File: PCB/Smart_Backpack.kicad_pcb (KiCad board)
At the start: 2 copper layers, 2 parts, among them J1 Power USB C Receptacle, U2 ICM-20602

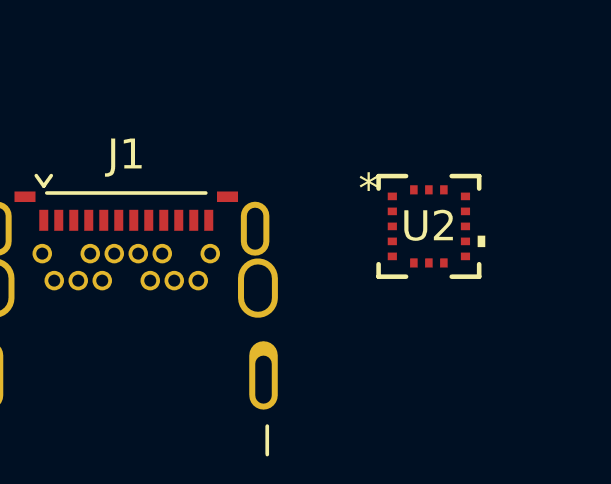
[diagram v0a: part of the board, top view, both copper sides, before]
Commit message: New IMU symbol/footprint
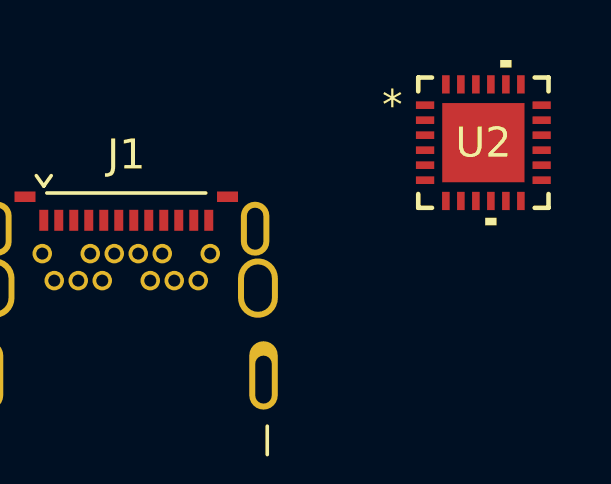
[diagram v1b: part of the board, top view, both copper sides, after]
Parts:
- U2: value ICM-20602 -> MPU-6050; footprint IMU:LGA16_I62_IVS-L -> IMU:QFN24_4X4X0P9-0P5_TDK-L
- moved U2 3.33 mm to (94.6, 74.9)

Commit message: Added micro footprint
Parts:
- added U3: ESP32-PICO-MINI-02-N8R2, STM32:ESP32-PICO-MINI-02_EXP, F.Cu at (57.6, 53.3)

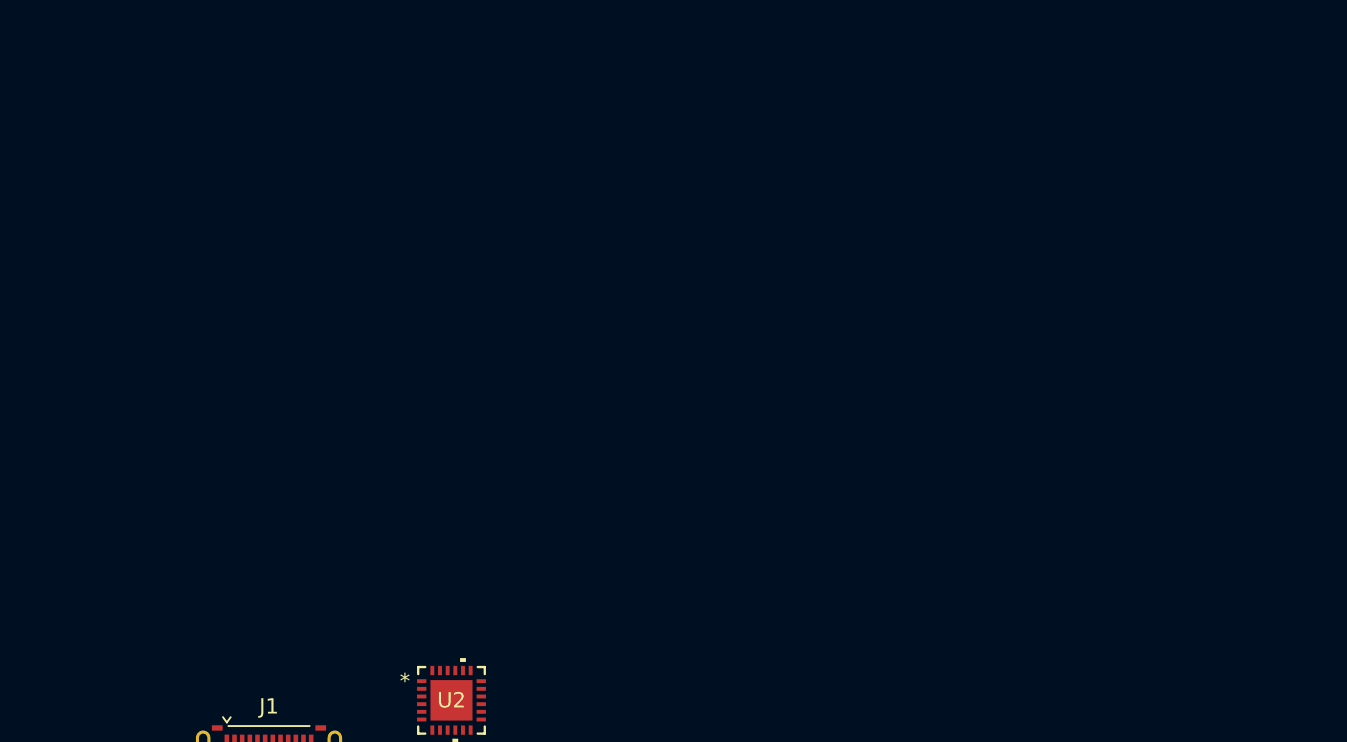
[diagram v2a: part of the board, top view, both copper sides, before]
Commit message: add pressure button and R, C, and L footprints
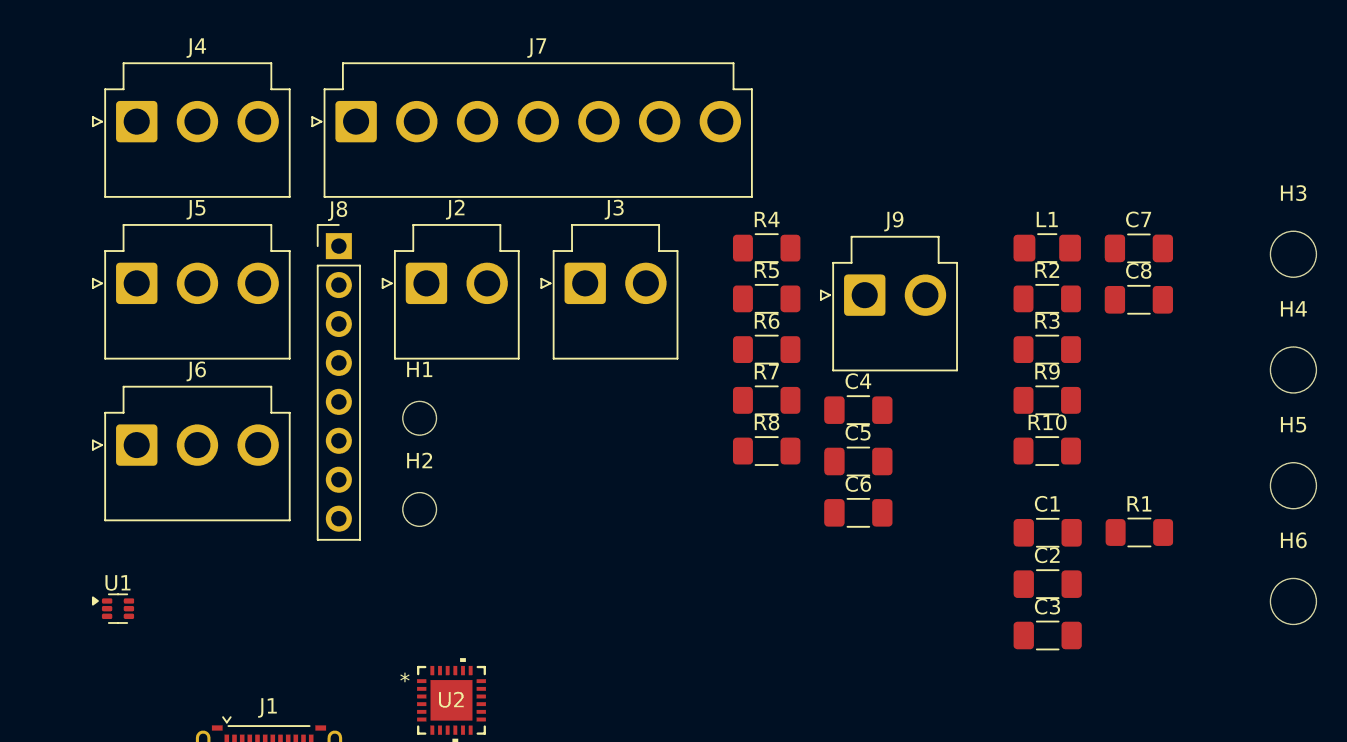
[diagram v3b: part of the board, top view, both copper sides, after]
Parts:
- added C1: 22uF, Capacitor_SMD:C_1206_3216Metric_Pad1.33x1.80mm_HandSolder, F.Cu at (133.5, 64.0)
- added C2: 0.1uF, Capacitor_SMD:C_1206_3216Metric_Pad1.33x1.80mm_HandSolder, F.Cu at (133.5, 67.4)
- added C3: 1uF, Capacitor_SMD:C_1206_3216Metric_Pad1.33x1.80mm_HandSolder, F.Cu at (133.5, 70.7)
- added C4: 2.2nF, Capacitor_SMD:C_1206_3216Metric_Pad1.33x1.80mm_HandSolder, F.Cu at (121.1, 56.0)
- added C5: 0.1uF, Capacitor_SMD:C_1206_3216Metric_Pad1.33x1.80mm_HandSolder, F.Cu at (121.1, 59.4)
- added C6: 10uF, Capacitor_SMD:C_1206_3216Metric_Pad1.33x1.80mm_HandSolder, F.Cu at (121.1, 62.7)
- added C7: 4.7uF, Capacitor_SMD:C_1206_3216Metric_Pad1.33x1.80mm_HandSolder, F.Cu at (139.4, 45.5)
- added C8: 22uF, Capacitor_SMD:C_1206_3216Metric_Pad1.33x1.80mm_HandSolder, F.Cu at (139.4, 48.8)
- added H1: MountingHole, MountingHole:MountingHole_2.2mm_M2, F.Cu at (92.5, 56.5)
- added H2: MountingHole, MountingHole:MountingHole_2.2mm_M2, F.Cu at (92.5, 62.5)
- added H3: MountingHole, MountingHole:MountingHole_3mm, F.Cu at (149.5, 45.9)
- added H4: MountingHole, MountingHole:MountingHole_3mm, F.Cu at (149.5, 53.4)
- added H5: MountingHole, MountingHole:MountingHole_3mm, F.Cu at (149.5, 61.0)
- added H6: MountingHole, MountingHole:MountingHole_3mm, F.Cu at (149.5, 68.5)
- added J2: Conn_01x02_Pin, Connector_JST:JST_VH_B2P-VH_1x02_P3.96mm_Vertical, F.Cu at (92.9, 47.8)
- added J3: Conn_01x02_Pin, Connector_JST:JST_VH_B2P-VH_1x02_P3.96mm_Vertical, F.Cu at (103.3, 47.8)
- added J4: Conn_01x03_Pin, Connector_JST:JST_VH_B3P-VH_1x03_P3.96mm_Vertical, F.Cu at (74.0, 37.2)
- added J5: Conn_01x03_Pin, Connector_JST:JST_VH_B3P-VH_1x03_P3.96mm_Vertical, F.Cu at (74.0, 47.8)
- added J6: Conn_01x03_Pin, Connector_JST:JST_VH_B3P-VH_1x03_P3.96mm_Vertical, F.Cu at (74.0, 58.3)
- added J7: Conn_01x07_Pin, Connector_JST:JST_VH_B7P-VH_1x07_P3.96mm_Vertical, F.Cu at (88.4, 37.2)
- added J8: Conn_01x08_Socket, Connector_PinHeader_2.54mm:PinHeader_1x08_P2.54mm_Vertical, F.Cu at (87.2, 45.3)
- added J9: Conn_01x02_Pin, Connector_JST:JST_VH_B2P-VH_1x02_P3.96mm_Vertical, F.Cu at (121.5, 48.5)
- added L1: 1uH, Inductor_SMD:L_1206_3216Metric_Pad1.42x1.75mm_HandSolder, F.Cu at (133.4, 45.5)
- added R1: 10 kΩ, Resistor_SMD:R_1206_3216Metric_Pad1.30x1.75mm_HandSolder, F.Cu at (139.4, 64.0)
- added R10: 5.1kΩ, Resistor_SMD:R_1206_3216Metric_Pad1.30x1.75mm_HandSolder, F.Cu at (133.4, 58.7)
- added R2: 5.1kΩ, Resistor_SMD:R_1206_3216Metric_Pad1.30x1.75mm_HandSolder, F.Cu at (133.4, 48.8)
- added R3: 5.1kΩ, Resistor_SMD:R_1206_3216Metric_Pad1.30x1.75mm_HandSolder, F.Cu at (133.4, 52.1)
- added R4: 10kΩ, Resistor_SMD:R_1206_3216Metric_Pad1.30x1.75mm_HandSolder, F.Cu at (115.1, 45.5)
- added R5: 10kΩ, Resistor_SMD:R_1206_3216Metric_Pad1.30x1.75mm_HandSolder, F.Cu at (115.1, 48.8)
- added R6: 10K, Resistor_SMD:R_1206_3216Metric_Pad1.30x1.75mm_HandSolder, F.Cu at (115.1, 52.1)
- added R7: 10K, Resistor_SMD:R_1206_3216Metric_Pad1.30x1.75mm_HandSolder, F.Cu at (115.1, 55.4)
- added R8: 10K, Resistor_SMD:R_1206_3216Metric_Pad1.30x1.75mm_HandSolder, F.Cu at (115.1, 58.7)
- added R9: 5.1kΩ, Resistor_SMD:R_1206_3216Metric_Pad1.30x1.75mm_HandSolder, F.Cu at (133.4, 55.4)
- added U1: TLV62569ADRL, Package_TO_SOT_SMD:SOT-563, F.Cu at (72.8, 69.0)
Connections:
- U2 pad 10: unconnected-(U2-REGOUT-Pad10) -> Net-(U2-REGOUT)
- U2 pad 12: unconnected-(U2-INT-Pad12) -> IMU_INT
- U2 pad 13: unconnected-(U2-VDD-Pad13) -> Buck_3v3
- U2 pad 18: unconnected-(U2-GND-Pad18) -> GND
- U2 pad 20: unconnected-(U2-CPOUT-Pad20) -> Net-(U2-CPOUT)
- U2 pad 23: unconnected-(U2-SCL-Pad23) -> ESP_SCL
- U2 pad 24: unconnected-(U2-SDA-Pad24) -> ESP_SDA
- U2 pad 25: unconnected-(U2-EPAD-Pad25) -> GND
- U2 pad 8: unconnected-(U2-VLOGIC-Pad8) -> Buck_3v3

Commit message: lots of 'final' schematic updates. ERC is essentially clean, PCB design can begin
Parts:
- added C10: 0.1uF, Capacitor_SMD:C_1206_3216Metric_Pad1.33x1.80mm_HandSolder, F.Cu at (182.2, 50.2)
- added C11: 0.1uF, Capacitor_SMD:C_1206_3216Metric_Pad1.33x1.80mm_HandSolder, F.Cu at (182.2, 53.6)
- added C12: 15pF, Capacitor_SMD:C_1206_3216Metric_Pad1.33x1.80mm_HandSolder, F.Cu at (156.0, 26.5)
- added C13: 15pF, Capacitor_SMD:C_1206_3216Metric_Pad1.33x1.80mm_HandSolder, F.Cu at (156.0, 29.9)
- added C9: 0.1uF, Capacitor_SMD:C_1206_3216Metric_Pad1.33x1.80mm_HandSolder, F.Cu at (193.5, 55.5)
- added D1: 3v3 Indicator, LED_SMD:LED_0603_1608Metric_Pad1.05x0.95mm_HandSolder, F.Cu at (181.4, 56.5)
- added D2: 5V Indicator, LED_SMD:LED_0603_1608Metric_Pad1.05x0.95mm_HandSolder, F.Cu at (181.4, 59.1)
- added J1: Conn_01x03_Pin, Connector_JST:JST_VH_B3P-VH_1x03_P3.96mm_Vertical, F.Cu at (193.9, 40.3)
- added R11: Minimum Resistance, Resistor_SMD:R_1206_3216Metric_Pad1.30x1.75mm_HandSolder, F.Cu at (192.9, 79.5)
- added R12: 5.1kΩ, Resistor_SMD:R_1206_3216Metric_Pad1.30x1.75mm_HandSolder, F.Cu at (207.6, 69.1)
- added R13: 5.1kΩ, Resistor_SMD:R_1206_3216Metric_Pad1.30x1.75mm_HandSolder, F.Cu at (207.6, 72.4)
- added R14: 47.5kΩ, Resistor_SMD:R_1206_3216Metric_Pad1.30x1.75mm_HandSolder, F.Cu at (207.6, 75.7)
- added R15: 1MΩ, Resistor_SMD:R_1206_3216Metric_Pad1.30x1.75mm_HandSolder, F.Cu at (207.6, 79.0)
- added R16: 10kΩ, Resistor_SMD:R_1206_3216Metric_Pad1.30x1.75mm_HandSolder, F.Cu at (207.6, 82.3)
- added R17: Minimum Resistance, Resistor_SMD:R_1206_3216Metric_Pad1.30x1.75mm_HandSolder, F.Cu at (207.6, 85.6)
- added R18: 10MΩ, Resistor_SMD:R_1206_3216Metric_Pad1.30x1.75mm_HandSolder, F.Cu at (201.4, 87.0)
- added R19: 150Ω, Resistor_SMD:R_1206_3216Metric_Pad1.30x1.75mm_HandSolder, F.Cu at (207.6, 88.9)
- added R20: 330Ω, Resistor_SMD:R_1206_3216Metric_Pad1.30x1.75mm_HandSolder, F.Cu at (207.6, 92.2)
- added RTC1: 32.768kHz, RTC:XTAL_AB38T-32.768KHZ-B7, F.Cu at (163.5, 22.5)
- added SW1: SW_Push, SMD_Button:Shop_SMD_Button, F.Cu at (195.1, 51.0)
- added SW2: SW_Push, SMD_Button:Shop_SMD_Button, F.Cu at (183.8, 38.5)
- added U4: CP2102N-Axx-xQFN28, Package_DFN_QFN:QFN-28-1EP_5x5mm_P0.5mm_EP3.35x3.35mm, F.Cu at (182.8, 44.9)
- R2: value 5.1kΩ -> 2kΩ
- R3: value 5.1kΩ -> 22.1kΩ
- moved R8 64.7 mm to (176.4, 79.5)
- moved R7 60.8 mm to (170.9, 79.5)
- moved R10 58.0 mm to (187.6, 79.5)
- moved R6 57.3 mm to (165.4, 79.5)
- moved R5 54.3 mm to (159.9, 79.5)
- moved R9 54.2 mm to (182.0, 79.5)
- moved R4 52.0 mm to (154.4, 79.5)
- moved R2 32.2 mm to (142.9, 79.5)
- moved R3 31.5 mm to (148.9, 79.5)
- moved R1 15.6 mm to (137.4, 79.5)
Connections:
- C1 pad 1: Buck_3v3 -> +3V3
- C2 pad 1: Buck_3v3 -> +3V3
- C6 pad 1: Buck_3v3 -> +3V3
- C7 pad 1: USB_5V -> +5V
- C8 pad 1: Buck_3v3 -> +3V3
- J2 pad 1: /Peripherals/FLEX_1 -> FLEX_1
- J3 pad 1: /Peripherals/FLEX_2 -> FLEX_2
- J4 pad 2: /Peripherals/MOIST_SIG -> MOIST_SIG
- J5 pad 2: /Peripherals/HALL_1 -> HALL_1
- J6 pad 2: /Peripherals/HALL_2 -> HALL_2
- J7 pad 2: /Peripherals/SS -> RFID_CS
- J7 pad 3: /Peripherals/SCK -> RFID_SCLK
- J7 pad 4: /Peripherals/MOSI -> RFID_MOSI
- J7 pad 5: /Peripherals/MISO -> RFID_MISO
- J7 pad 6: /Peripherals/SPI_RST -> RFID_RST
- J8 pad 5: unconnected-(J8-Pin_5-Pad5) -> GPS_TX
- J8 pad 6: unconnected-(J8-Pin_6-Pad6) -> GPS_RX
- J8 pad 7: unconnected-(J8-Pin_7-Pad7) -> GND
- J8 pad 8: unconnected-(J8-Pin_8-Pad8) -> +3V3
- L1 pad 2: Buck_3v3 -> +3V3
- R1 pad 1: Buck_3v3 -> +3V3
- R2 pad 1: Net-(J1-CC1) -> +3V3
- R2 pad 2: GND -> Net-(U4-~{RST})
- R3 pad 1: Net-(J1-CC2) -> Net-(U4-VBUS)
- R3 pad 2: GND -> +5V
- R4 pad 1: Buck_3v3 -> +3V3
- R4 pad 2: ESP_SDA -> IMU_SDA
- R5 pad 1: Buck_3v3 -> +3V3
- R5 pad 2: ESP_SCL -> IMU_SCL
- R6 pad 1: /Peripherals/FLEX_1 -> FLEX_1
- R7 pad 1: /Peripherals/FLEX_2 -> FLEX_2
- R8 pad 1: /Peripherals/MOIST_SIG -> MOIST_SIG
- R9 pad 1: Buck_3v3 -> +3V3
- U1 pad 3: USB_5V -> +5V
- U1 pad 5: USB_5V -> +5V
- U2 pad 13: Buck_3v3 -> +3V3
- U2 pad 23: ESP_SCL -> IMU_SCL
- U2 pad 24: ESP_SDA -> IMU_SDA
- U2 pad 8: Buck_3v3 -> +3V3
- U3 pad 10: unconnected-(U3-I35-Pad10) -> MOIST_SIG
- U3 pad 12: unconnected-(U3-IO32-Pad12) -> RTC_XP
- U3 pad 13: unconnected-(U3-IO33-Pad13) -> RTC_XN
- U3 pad 15: unconnected-(U3-IO25-Pad15) -> LAPTOP
- U3 pad 17: unconnected-(U3-IO27-Pad17) -> RFID_RST
- U3 pad 18: unconnected-(U3-IO14-Pad18) -> RFID_SCLK
- U3 pad 19: unconnected-(U3-IO12-Pad19) -> RFID_MISO
- U3 pad 20: unconnected-(U3-IO13-Pad20) -> RFID_MOSI
- U3 pad 21: unconnected-(U3-IO15-Pad21) -> RFID_CS
- U3 pad 23: unconnected-(U3-IO0-Pad23) -> IO0
- U3 pad 26: unconnected-(U3-IO20-Pad26) -> IMU_SCL
- U3 pad 27: unconnected-(U3-IO7-Pad27) -> GPS_TX
- U3 pad 28: unconnected-(U3-IO8-Pad28) -> GPS_RX
- U3 pad 3: Buck_3v3 -> +3V3
- U3 pad 30: unconnected-(U3-RXD0-Pad30) -> Flash_TXD
- U3 pad 31: unconnected-(U3-TXD0-Pad31) -> Flash_RXD
- U3 pad 34: unconnected-(U3-IO22-Pad34) -> IMU_SDA
- U3 pad 4: unconnected-(U3-I36-Pad4) -> HALL_1
- U3 pad 5: unconnected-(U3-I37-Pad5) -> HALL_2
- U3 pad 6: unconnected-(U3-I38-Pad6) -> FLEX_1
- U3 pad 7: unconnected-(U3-I39-Pad7) -> FLEX_2

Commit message: Finally PCB progress
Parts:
- removed the J1 at (82.7, 80.8)
- J9: value Conn_01x02_Pin -> USB_C_Receptacle_USB2.0_16P; footprint Connector_JST:JST_VH_B2P-VH_1x02_P3.96mm_Vertical -> Connector_USB:USB_C_Receptacle_G-Switch_GT-USB-7010ASV
- R11, R17: value Minimum Resistance -> 5Ω
- moved R15 130.6 mm to (82.8, 117.9), turned to 90 degrees
- moved R13 122.9 mm to (92.3, 115.1)
- moved R12 122.0 mm to (90.5, 103.4), turned to 90 degrees
- moved R20 120.2 mm to (87.6, 101.1), turned to 90 degrees
- moved R19 112.0 mm to (101.0, 123.2), turned to -90 degrees
- moved R14 110.9 mm to (101.5, 108.0), turned to 180 degrees
- moved U4 110.0 mm to (93.5, 109.1)
- moved R16 108.1 mm to (101.5, 102.9)
- moved R10 106.9 mm to (88.3, 119.2), turned to 180 degrees
- moved C10 102.5 mm to (101.5, 113.3), turned to 180 degrees
- moved R9 102.5 mm to (89.3, 123.2), turned to 90 degrees
- moved D1 101.8 mm to (104.5, 123.2), turned to -90 degrees
- moved D2 98.3 mm to (91.7, 99.3), turned to 180 degrees
- moved U3 88.5 mm to (126.0, 109.4), turned to 180 degrees
- moved L1 87.6 mm to (93.1, 123.2), turned to -90 degrees
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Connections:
- R12 pad 1: Net-(J10-CC1) -> Net-(J9-CC1)
- R13 pad 1: Net-(J10-CC2) -> Net-(J9-CC2)
- R15 pad 2: Net-(J10-SHIELD) -> Net-(J9-SHIELD)
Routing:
- net +3V3: track 0.00 -> 68.9 mm
- net +5V: track 0.00 -> 37.2 mm
- net Flash_TXD: track 0.00 -> 32.6 mm
- net Flash_RXD: track 0.00 -> 32.0 mm
- net Net-(J9-SHIELD): track 0.00 -> 19.3 mm
- net Net-(U4-~{SUSPEND}): track 0.00 -> 14.3 mm
- net Net-(U4-~{RST}): track 0.00 -> 14.0 mm
- net Net-(U4-VBUS): track 0.00 -> 13.2 mm
- net Net-(U4-VDD): track 0.00 -> 11.9 mm
- net USB_D+: track 0.00 -> 6.66 mm, vias 0 -> 2
- net USB_D-: track 0.00 -> 6.45 mm
- net Net-(J9-CC2): track 0.00 -> 5.43 mm
- net Net-(J9-CC1): track 0.00 -> 5.25 mm
- net Net-(U1-FB): track 0.00 -> 5.01 mm
- net Net-(D1-A): track 0.00 -> 3.80 mm
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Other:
- board text added: "3.3V LED"
- board text added: "5V LED"

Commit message: bit more PCB progress, added buttons and filter
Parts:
- moved R17 88.5 mm to (119.9, 97.3)
- moved SW2 82.5 mm to (120.1, 90.9)
- moved C11 74.7 mm to (119.9, 94.7)
- moved SW1 73.1 mm to (143.8, 103.1), turned to -90 degrees
- moved RTC1 72.8 mm to (132.6, 88.4), turned to 180 degrees
- moved C9 71.6 mm to (140.2, 103.4), turned to -90 degrees
- moved C12 71.1 mm to (133.6, 94.0), turned to -90 degrees
- moved R18 70.0 mm to (132.3, 98.0), turned to 180 degrees
- moved C13 68.9 mm to (130.8, 94.0), turned to -90 degrees
- moved R11 60.2 mm to (137.7, 103.4), turned to -90 degrees
- moved C1 50.3 mm to (135.4, 114.3), turned to -90 degrees
- moved C2 47.1 mm to (137.9, 114.3), turned to -90 degrees
- moved R1 34.9 mm to (140.5, 114.3), turned to 90 degrees
- moved C3 32.7 mm to (135.1, 103.4), turned to 90 degrees
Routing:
- net RTC_XP: track 0.00 -> 17.5 mm
- net RTC_XN: track 0.00 -> 16.5 mm
- net ESP_EN: track 0.00 -> 14.8 mm, vias 0 -> 2
- net +3V3: track 68.9 -> 77.7 mm
- net Net-(C9-Pad1): track 0.00 -> 5.11 mm
- net Net-(C11-Pad1): track 0.00 -> 4.91 mm
- net IO0: track 0.00 -> 4.80 mm
